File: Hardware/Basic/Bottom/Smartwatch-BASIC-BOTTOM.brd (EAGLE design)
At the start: 33 x 33 mm, 37 parts, among them U1 AD5242-SO16, U3 PCF8523

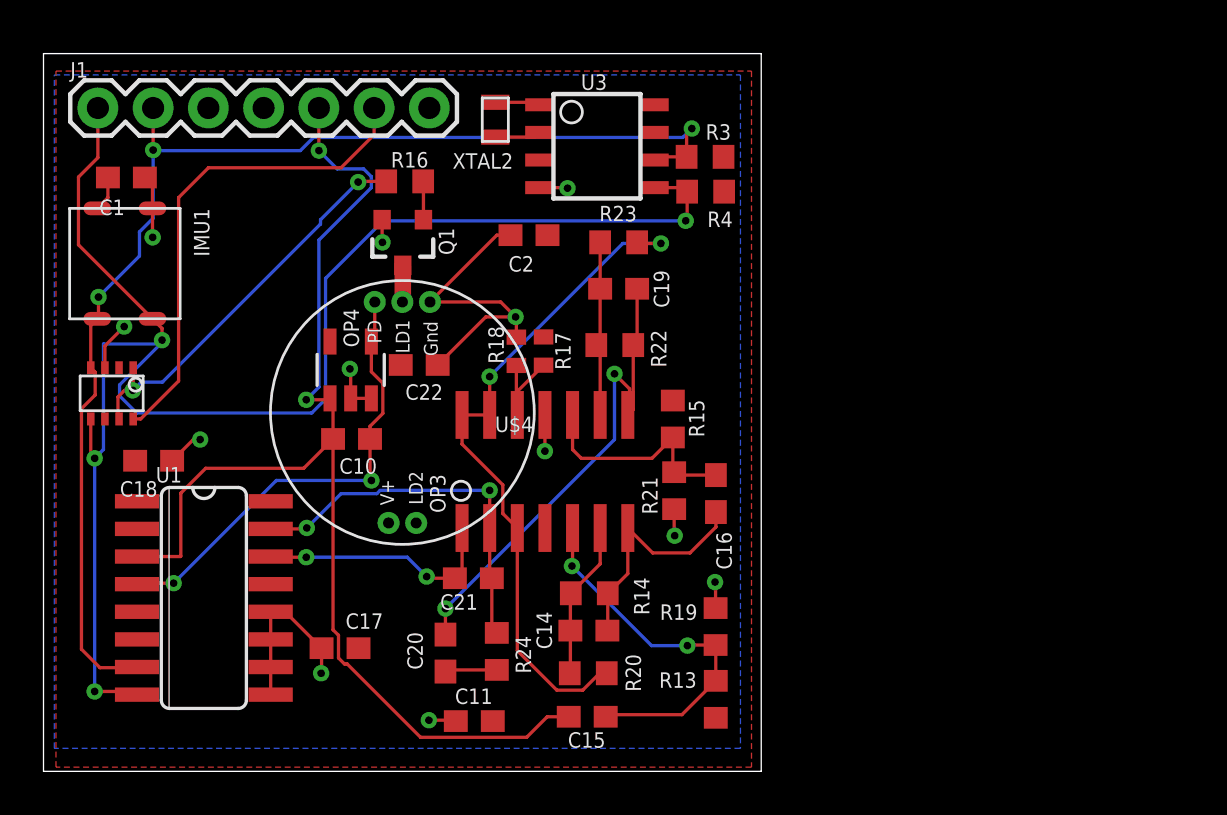
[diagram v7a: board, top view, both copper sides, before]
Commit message: Fixed Bottom Board Mistakes
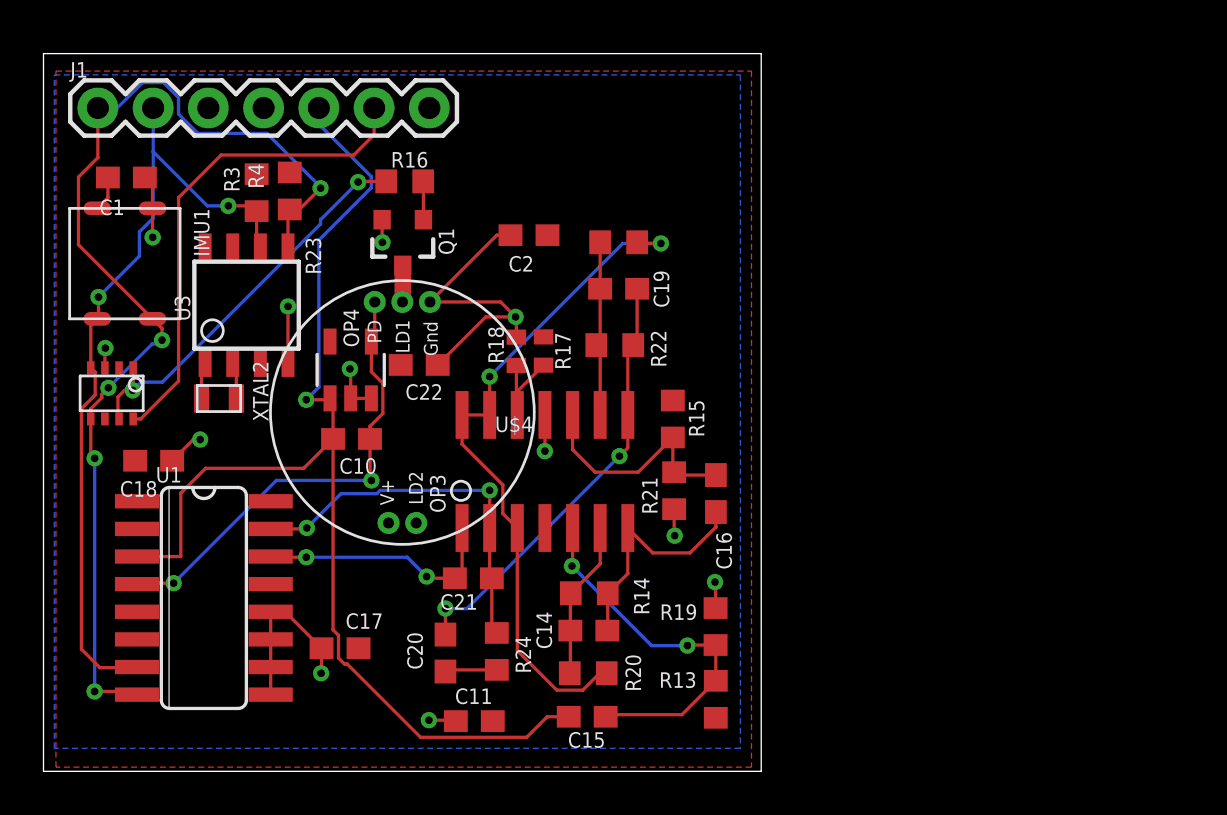
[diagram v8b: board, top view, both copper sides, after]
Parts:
- moved R3 20.7 mm to (12.3, 29.1), turned to 90 degrees
- moved R4 19.1 mm to (13.8, 29.2), turned to 90 degrees
- moved XTAL2 18.1 mm to (10.6, 19.6), turned to 180 degrees
- moved U3 17.7 mm to (11.8, 23.9), turned to 90 degrees
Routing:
- net SDA: track 75.0 -> 49.2 mm, vias 4 -> 5
- net SCL: track 57.5 -> 37.0 mm, vias 3 -> 2
- net N$19: track 23.5 -> 20.3 mm
- net A6/TIA: track 55.0 -> 54.3 mm, vias 2 -> 1
- net N$17: track 10.4 -> 10.9 mm
